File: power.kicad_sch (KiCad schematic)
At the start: 4 parts, among them J22 Conn_01x02_Socket, U8 AZ1117-3.3

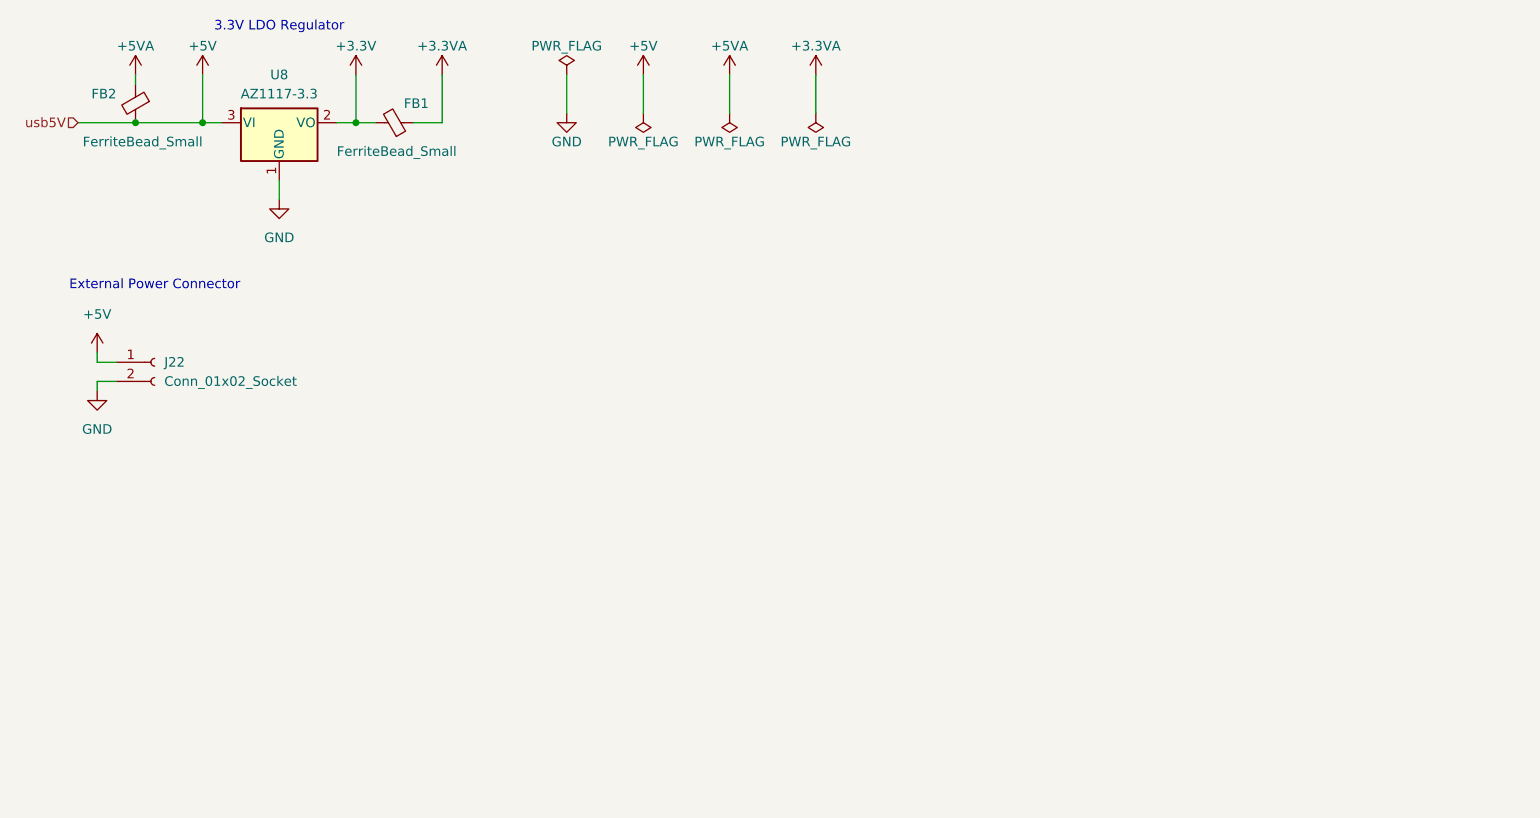
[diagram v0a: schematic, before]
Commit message: added power mux, finished up schematic and picking footprints/partnumbers
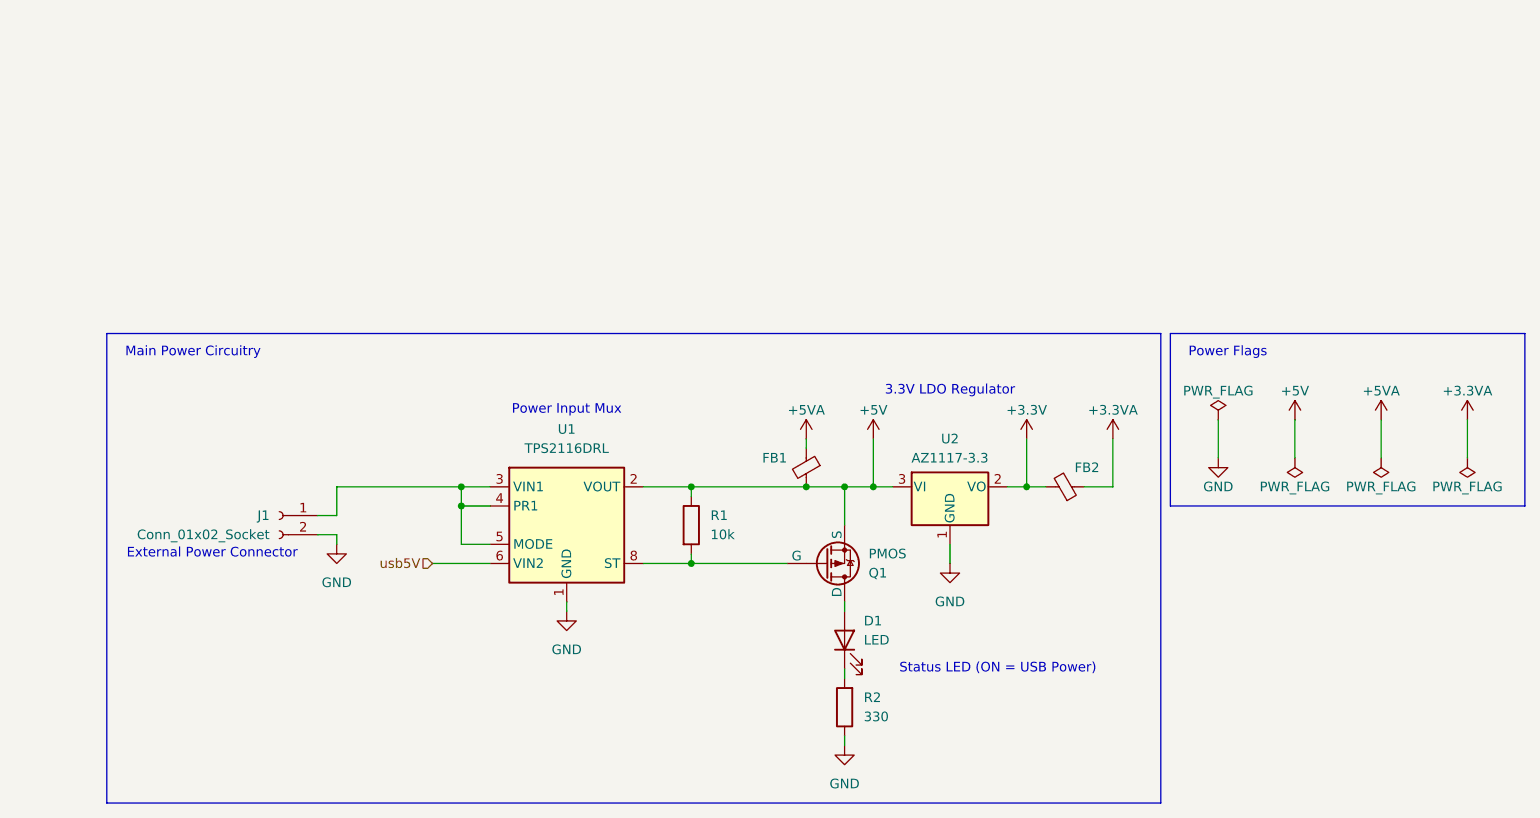
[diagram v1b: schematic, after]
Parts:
- added D1: LED, Resistor_SMD:R_0603_1608Metric, symbol Device:LED
- added Q1: PMOS, Package_TO_SOT_THT:TO-92_HandSolder, symbol Simulation_SPICE:PMOS
- added R1: 10k, symbol Device:R
- added R2: 330, Resistor_SMD:R_0805_2012Metric, symbol Device:R
- added U1: TPS2116DRL, Package_TO_SOT_SMD:SOT-583-8, symbol Power_Management:TPS2116DRL
- U2: renamed from U8; footprint (none) -> Package_TO_SOT_SMD:SOT-223; DKPN (none) -> AZ1117CH-3.3TRG1DICT-ND
- renumbered FB2 to FB1, FB1 to FB2, J22 to J1
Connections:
- net +5V: now also Q1.3 (S), R1.1, U1.2 (VOUT), U1.7 (VOUT); no longer J1.1 (Pin_1)
- net GND: now also R2.1, U1.1 (GND)
- new net: J1.1 (Pin_1), U1.3 (VIN1), U1.4 (PR1), U1.5 (MODE)
- new net: Q1.2 (G), R1.2, U1.8 (ST)
- new net: D1.1 (K), R2.2
- new net: D1.2 (A), Q1.1 (D)
- new net usb5V: U1.6 (VIN2)
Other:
- note added: "Main Power Circuitry"
- note added: "Power Flags"
- note added: "Power Input Mux"
- note added: "Status LED (ON = USB Power)"
- moved on the sheet: FB1, FB2, J1, U2

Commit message: forgot to add footprints for 10k resistors
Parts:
- R1: footprint (none) -> Resistor_SMD:R_0805_2012Metric
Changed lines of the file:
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@@
 			)
 		)
-		(property "Footprint" ""
+		(property "Footprint" "Resistor_SMD:R_0805_2012Metric"
 			(at 150.622 100.33 90)
 			(hide yes)

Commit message: fix final footprint picking issues
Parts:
- Q1: footprint Package_TO_SOT_THT:TO-92_HandSolder -> Package_TO_SOT_SMD:SOT-23; DKPN ZVP3306A-ND -> BSS84PH6327XTSA2CT-ND
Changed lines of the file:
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@@
 			)
 		)
-		(property "Footprint" "Package_TO_SOT_THT:TO-92_HandSolder"
+		(property "Footprint" "Package_TO_SOT_SMD:SOT-23"
 			(at 175.26 107.95 0)
 			(hide yes)
@@
 			)
 		)
-		(property "DKPN" "ZVP3306A-ND"
+		(property "DKPN" "BSS84PH6327XTSA2CT-ND"
 			(at 170.18 105.41 0)
 			(hide yes)
